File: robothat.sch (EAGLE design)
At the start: 84 parts, among them IC3 78L05SMD, T1 BC847, U1 LM293AD, U2 TSM2312CX, U3 ADUM7441ARQZ, U5 TSM2312CX, U8 LM293AD

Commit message: finished first place
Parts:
- removed C3: 100n, rcl:C-EUC0805
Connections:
- net AGND: no longer C3.1
- net AX12_RX: now also AXFUSE1.2
- net AX12_RX_P: no longer AXFUSE1.2
- net VCC: no longer C3.2
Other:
- moved on the sheet: AXFUSE, AXFUSE1
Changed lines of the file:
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@@
 <setting verticaltext="up"/>
 </settings>
-<grid distance="0.1" unitdist="inch" unit="inch" style="lines" multiple="1" display="no" altdistance="0.01" altunitdist="inch" altunit="inch"/>
+<grid distance="0.05" unitdist="inch" unit="inch" style="lines" multiple="1" display="no" altdistance="0.01" altunitdist="inch" altunit="inch"/>
 <layers>
 <layer number="1" name="Top" color="4" fill="1" visible="no" active="no"/>
@@
 <part name="R6" library="resistor" deviceset="R-US_" device="R0805" value="470R"/>
 <part name="R7" library="resistor" deviceset="R-US_" device="R0805" value="470R"/>
-<part name="C3" library="rcl" deviceset="C-EU" device="C0805" value="100n"/>
 <part name="GND4" library="supply1" deviceset="GND" device=""/>
 <part name="POWER" library="con-phoenix-500" deviceset="MSTBV2" device=""/>
@@
 <part name="P+22" library="supply1" deviceset="VCC" device=""/>
 <part name="P+23" library="supply1" deviceset="VCC" device=""/>
-<part name="AGND10" library="supply1" deviceset="AGND" device=""/>
 <part name="VDD1" library="supply1" deviceset="VDD" device=""/>
 <part name="VDD2" library="supply1" deviceset="VDD" device=""/>
@@
 <instance part="R6" gate="G$1" x="424.18" y="177.8" rot="R180"/>
 <instance part="R7" gate="G$1" x="424.18" y="185.42" rot="R180"/>
-<instance part="C3" gate="G$1" x="378.46" y="190.5" rot="R180"/>
 <instance part="GND4" gate="1" x="24.13" y="130.81"/>
 <instance part="POWER" gate="-1" x="281.94" y="193.04" rot="R270"/>
@@
 <instance part="GND16" gate="1" x="215.9" y="35.56"/>
 <instance part="C13" gate="G$1" x="251.46" y="43.18" rot="R180"/>
-<instance part="AXFUSE" gate="G$1" x="208.28" y="91.44" rot="R90"/>
-<instance part="AXFUSE1" gate="G$1" x="213.36" y="78.74" rot="R90"/>
+<instance part="AXFUSE" gate="G$1" x="147.32" y="157.48"/>
+<instance part="AXFUSE1" gate="G$1" x="148.59" y="165.1"/>
 <instance part="AGND1" gate="VR1" x="241.3" y="35.56"/>
 <instance part="AGND2" gate="VR1" x="251.46" y="35.56"/>
@@
 <instance part="P+22" gate="VCC" x="254" y="177.8"/>
 <instance part="P+23" gate="VCC" x="256.54" y="114.3"/>
-<instance part="AGND10" gate="VR1" x="378.46" y="182.88"/>
 <instance part="VDD1" gate="G$1" x="330.2" y="142.24"/>
 <instance part="VDD2" gate="G$1" x="292.1" y="187.96"/>
@@
 <segment>
 <pinref part="U3" gate="A" pin="VOC"/>
-<wire x1="213.36" y1="101.6" x2="210.82" y2="101.6" width="0.1524" layer="91"/>
 <label x="195.58" y="101.6" size="1.778" layer="95"/>
-<pinref part="AXFUSE1" gate="G$1" pin="2"/>
-<wire x1="210.82" y1="101.6" x2="208.28" y2="101.6" width="0.1524" layer="91"/>
-<wire x1="213.36" y1="83.82" x2="213.36" y2="96.52" width="0.1524" layer="91"/>
-<wire x1="213.36" y1="96.52" x2="210.82" y2="96.52" width="0.1524" layer="91"/>
-<wire x1="210.82" y1="96.52" x2="210.82" y2="101.6" width="0.1524" layer="91"/>
-<junction x="210.82" y="101.6"/>
+<wire x1="213.36" y1="101.6" x2="208.28" y2="101.6" width="0.1524" layer="91"/>
 </segment>
 </net>
@@
 <segment>
 <pinref part="AXFUSE1" gate="G$1" pin="1"/>
-<wire x1="213.36" y1="73.66" x2="205.74" y2="73.66" width="0.1524" layer="91"/>
-<label x="195.58" y="73.66" size="1.778" layer="95" ratio="12"/>
+<wire x1="143.51" y1="165.1" x2="139.7" y2="165.1" width="0.1524" layer="91"/>
+<label x="129.54" y="165.1" size="1.778" layer="95" ratio="12"/>
 </segment>
 </net>
@@
 <segment>
 <pinref part="AXFUSE" gate="G$1" pin="1"/>
-<wire x1="208.28" y1="86.36" x2="205.74" y2="86.36" width="0.1524" layer="91"/>
-<label x="195.58" y="86.36" size="1.778" layer="95" ratio="12"/>
+<wire x1="142.24" y1="157.48" x2="139.7" y2="157.48" width="0.1524" layer="91"/>
+<label x="129.54" y="157.48" size="1.778" layer="95" ratio="12"/>
 </segment>
 </net>
@@
 <segment>
 <pinref part="AX12USB" gate="-1" pin="1"/>
-<wire x1="154.94" y1="149.86" x2="149.86" y2="149.86" width="0.1524" layer="91"/>
+<wire x1="154.94" y1="149.86" x2="152.4" y2="149.86" width="0.1524" layer="91"/>
 <label x="139.7" y="149.86" size="1.778" layer="95"/>
+<pinref part="AXFUSE" gate="G$1" pin="2"/>
+<wire x1="152.4" y1="149.86" x2="149.86" y2="149.86" width="0.1524" layer="91"/>
+<wire x1="152.4" y1="157.48" x2="152.4" y2="149.86" width="0.1524" layer="91"/>
+<junction x="152.4" y="149.86"/>
 </segment>
 <segment>
@@
 <wire x1="213.36" y1="99.06" x2="208.28" y2="99.06" width="0.1524" layer="91"/>
 <label x="198.12" y="99.06" size="1.778" layer="95"/>
-<pinref part="AXFUSE" gate="G$1" pin="2"/>
-<wire x1="208.28" y1="96.52" x2="208.28" y2="99.06" width="0.1524" layer="91"/>
 </segment>
 </net>
@@
 <segment>
 <pinref part="AX12USB" gate="-2" pin="1"/>
-<wire x1="154.94" y1="147.32" x2="149.86" y2="147.32" width="0.1524" layer="91"/>
+<wire x1="154.94" y1="147.32" x2="153.67" y2="147.32" width="0.1524" layer="91"/>
 <label x="139.7" y="147.32" size="1.778" layer="95"/>
+<pinref part="AXFUSE1" gate="G$1" pin="2"/>
+<wire x1="153.67" y1="147.32" x2="149.86" y2="147.32" width="0.1524" layer="91"/>
+<wire x1="153.67" y1="165.1" x2="153.67" y2="147.32" width="0.1524" layer="91"/>
+<junction x="153.67" y="147.32"/>
 </segment>
 <segment>
@@
 <pinref part="AGND9" gate="VR1" pin="AGND"/>
 </segment>
-<segment>
-<pinref part="C3" gate="G$1" pin="1"/>
-<wire x1="378.46" y1="187.96" x2="378.46" y2="185.42" width="0.1524" layer="91"/>
-<pinref part="AGND10" gate="VR1" pin="AGND"/>
-</segment>
 </net>
 <net name="VCC" class="0">
@@
 <pinref part="R3" gate="G$1" pin="2"/>
 <wire x1="365.76" y1="195.58" x2="365.76" y2="198.12" width="0.1524" layer="91"/>
-<wire x1="365.76" y1="198.12" x2="378.46" y2="198.12" width="0.1524" layer="91"/>
+<wire x1="365.76" y1="198.12" x2="383.54" y2="198.12" width="0.1524" layer="91"/>
 <pinref part="U1" gate="A" pin="VCC"/>
-<wire x1="378.46" y1="198.12" x2="383.54" y2="198.12" width="0.1524" layer="91"/>
 <wire x1="383.54" y1="182.88" x2="383.54" y2="198.12" width="0.1524" layer="91"/>
-<pinref part="C3" gate="G$1" pin="2"/>
-<wire x1="378.46" y1="195.58" x2="378.46" y2="198.12" width="0.1524" layer="91"/>
-<junction x="378.46" y="198.12"/>
 <pinref part="P+21" gate="VCC" pin="VCC"/>
 <junction x="383.54" y="198.12"/>

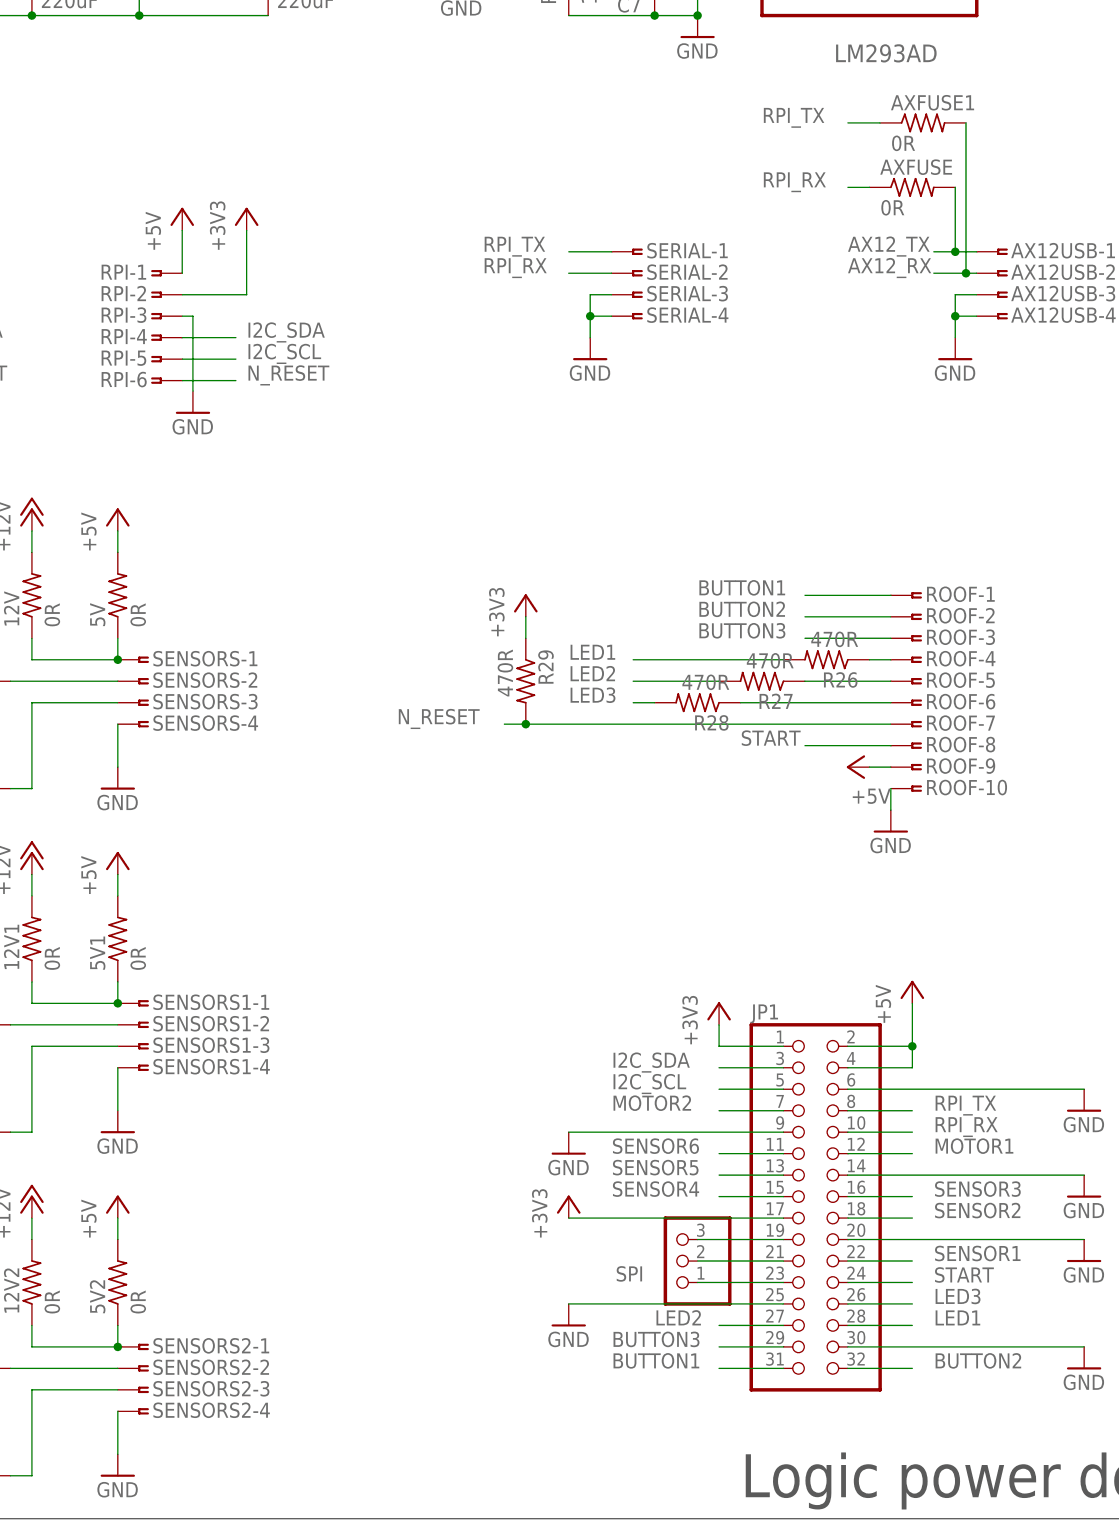
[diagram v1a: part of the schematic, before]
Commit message: routing and silkscreen done
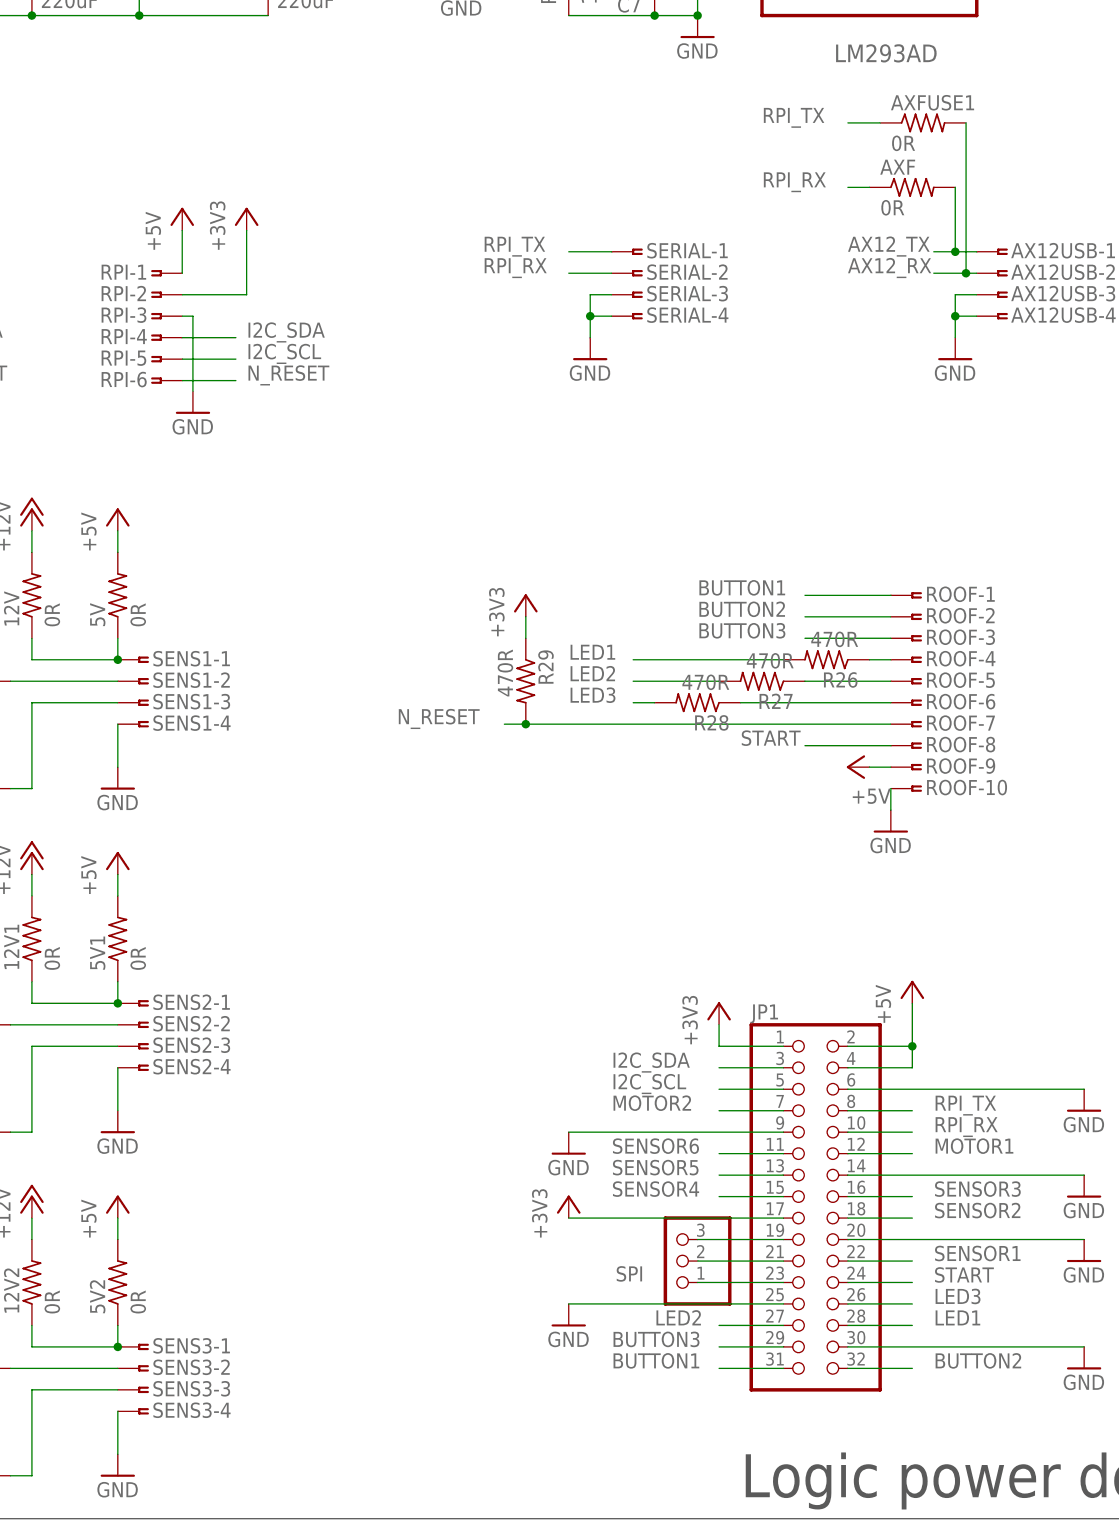
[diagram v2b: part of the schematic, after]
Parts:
- renumbered AXFUSE to AXF, SENSORS to SENS1, SENSORS1 to SENS2, SENSORS2 to SENS3
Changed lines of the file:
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@@
 <part name="AX12USB" library="con-amp" deviceset="SMDTOP-4" device=""/>
 <part name="GND7" library="supply1" deviceset="GND" device=""/>
-<part name="SENSORS" library="con-amp" deviceset="SMDTOP-4" device=""/>
+<part name="SENS1" library="con-amp" deviceset="SMDTOP-4" device=""/>
 <part name="12V" library="resistor" deviceset="R-US_" device="R0805" value="0R"/>
 <part name="P+8" library="supply1" deviceset="+12V" device=""/>
@@
 <part name="D1" library="diode" deviceset="DIODE-" device="SOD523"/>
 <part name="+3V4" library="supply1" deviceset="+3V3" device=""/>
-<part name="SENSORS1" library="con-amp" deviceset="SMDTOP-4" device=""/>
+<part name="SENS2" library="con-amp" deviceset="SMDTOP-4" device=""/>
 <part name="12V1" library="resistor" deviceset="R-US_" device="R0805" value="0R"/>
 <part name="P+12" library="supply1" deviceset="+12V" device=""/>
@@
 <part name="D4" library="diode" deviceset="DIODE-" device="SOD523"/>
 <part name="+3V6" library="supply1" deviceset="+3V3" device=""/>
-<part name="SENSORS2" library="con-amp" deviceset="SMDTOP-4" device=""/>
+<part name="SENS3" library="con-amp" deviceset="SMDTOP-4" device=""/>
 <part name="12V2" library="resistor" deviceset="R-US_" device="R0805" value="0R"/>
 <part name="P+17" library="supply1" deviceset="+12V" device=""/>
@@
 <part name="GND16" library="supply1" deviceset="GND" device=""/>
 <part name="C13" library="rcl" deviceset="C-EU" device="C0805" value="100n"/>
-<part name="AXFUSE" library="resistor" deviceset="R-US_" device="R0805" value="0R"/>
+<part name="AXF" library="resistor" deviceset="R-US_" device="R0805" value="0R"/>
 <part name="AXFUSE1" library="resistor" deviceset="R-US_" device="R0805" value="0R"/>
 <part name="AGND1" library="supply1" deviceset="AGND" device=""/>
@@
 <instance part="AX12USB" gate="-4" x="157.48" y="142.24"/>
 <instance part="GND7" gate="1" x="152.4" y="137.16"/>
-<instance part="SENSORS" gate="-1" x="55.88" y="101.6"/>
-<instance part="SENSORS" gate="-2" x="55.88" y="99.06"/>
-<instance part="SENSORS" gate="-3" x="55.88" y="96.52"/>
-<instance part="SENSORS" gate="-4" x="55.88" y="93.98"/>
+<instance part="SENS1" gate="-1" x="55.88" y="101.6"/>
+<instance part="SENS1" gate="-2" x="55.88" y="99.06"/>
+<instance part="SENS1" gate="-3" x="55.88" y="96.52"/>
+<instance part="SENS1" gate="-4" x="55.88" y="93.98"/>
 <instance part="12V" gate="G$1" x="43.18" y="109.22" rot="R90"/>
 <instance part="P+8" gate="1" x="43.18" y="119.38"/>
@@
 <instance part="D1" gate="G$1" x="27.94" y="101.6" rot="R90"/>
 <instance part="+3V4" gate="G$1" x="27.94" y="109.22"/>
-<instance part="SENSORS1" gate="-1" x="55.88" y="60.96"/>
-<instance part="SENSORS1" gate="-2" x="55.88" y="58.42"/>
-<instance part="SENSORS1" gate="-3" x="55.88" y="55.88"/>
-<instance part="SENSORS1" gate="-4" x="55.88" y="53.34"/>
+<instance part="SENS2" gate="-1" x="55.88" y="60.96"/>
+<instance part="SENS2" gate="-2" x="55.88" y="58.42"/>
+<instance part="SENS2" gate="-3" x="55.88" y="55.88"/>
+<instance part="SENS2" gate="-4" x="55.88" y="53.34"/>
 <instance part="12V1" gate="G$1" x="43.18" y="68.58" rot="R90"/>
 <instance part="P+12" gate="1" x="43.18" y="78.74"/>
@@
 <instance part="D4" gate="G$1" x="27.94" y="60.96" rot="R90"/>
 <instance part="+3V6" gate="G$1" x="27.94" y="68.58"/>
-<instance part="SENSORS2" gate="-1" x="55.88" y="20.32"/>
-<instance part="SENSORS2" gate="-2" x="55.88" y="17.78"/>
-<instance part="SENSORS2" gate="-3" x="55.88" y="15.24"/>
-<instance part="SENSORS2" gate="-4" x="55.88" y="12.7"/>
+<instance part="SENS3" gate="-1" x="55.88" y="20.32"/>
+<instance part="SENS3" gate="-2" x="55.88" y="17.78"/>
+<instance part="SENS3" gate="-3" x="55.88" y="15.24"/>
+<instance part="SENS3" gate="-4" x="55.88" y="12.7"/>
 <instance part="12V2" gate="G$1" x="43.18" y="27.94" rot="R90"/>
 <instance part="P+17" gate="1" x="43.18" y="38.1"/>
@@
 <instance part="GND16" gate="1" x="215.9" y="35.56"/>
 <instance part="C13" gate="G$1" x="251.46" y="43.18" rot="R180"/>
-<instance part="AXFUSE" gate="G$1" x="147.32" y="157.48"/>
+<instance part="AXF" gate="G$1" x="147.32" y="157.48"/>
 <instance part="AXFUSE1" gate="G$1" x="148.59" y="165.1"/>
 <instance part="AGND1" gate="VR1" x="241.3" y="35.56"/>
@@
 <segment>
 <pinref part="GND8" gate="1" pin="GND"/>
-<pinref part="SENSORS" gate="-4" pin="1"/>
+<pinref part="SENS1" gate="-4" pin="1"/>
 <wire x1="53.34" y1="88.9" x2="53.34" y2="93.98" width="0.1524" layer="91"/>
 </segment>
 <segment>
 <pinref part="GND9" gate="1" pin="GND"/>
-<pinref part="SENSORS1" gate="-4" pin="1"/>
+<pinref part="SENS2" gate="-4" pin="1"/>
 <wire x1="53.34" y1="48.26" x2="53.34" y2="53.34" width="0.1524" layer="91"/>
 </segment>
 <segment>
 <pinref part="GND10" gate="1" pin="GND"/>
-<pinref part="SENSORS2" gate="-4" pin="1"/>
+<pinref part="SENS3" gate="-4" pin="1"/>
 <wire x1="53.34" y1="7.62" x2="53.34" y2="12.7" width="0.1524" layer="91"/>
 </segment>
@@
 </segment>
 <segment>
-<pinref part="AXFUSE" gate="G$1" pin="1"/>
+<pinref part="AXF" gate="G$1" pin="1"/>
 <wire x1="142.24" y1="157.48" x2="139.7" y2="157.48" width="0.1524" layer="91"/>
 <label x="129.54" y="157.48" size="1.778" layer="95" ratio="12"/>
@@
 <wire x1="154.94" y1="149.86" x2="152.4" y2="149.86" width="0.1524" layer="91"/>
 <label x="139.7" y="149.86" size="1.778" layer="95"/>
-<pinref part="AXFUSE" gate="G$1" pin="2"/>
+<pinref part="AXF" gate="G$1" pin="2"/>
 <wire x1="152.4" y1="149.86" x2="149.86" y2="149.86" width="0.1524" layer="91"/>
 <wire x1="152.4" y1="157.48" x2="152.4" y2="149.86" width="0.1524" layer="91"/>
@@
 <net name="N$9" class="0">
 <segment>
-<pinref part="SENSORS" gate="-1" pin="1"/>
+<pinref part="SENS1" gate="-1" pin="1"/>
 <pinref part="12V" gate="G$1" pin="1"/>
 <wire x1="53.34" y1="101.6" x2="43.18" y2="101.6" width="0.1524" layer="91"/>
@@
 <segment>
 <pinref part="R19" gate="G$1" pin="1"/>
-<pinref part="SENSORS" gate="-2" pin="1"/>
+<pinref part="SENS1" gate="-2" pin="1"/>
 <wire x1="40.64" y1="99.06" x2="53.34" y2="99.06" width="0.1524" layer="91"/>
 </segment>
@@
 <wire x1="40.64" y1="86.36" x2="43.18" y2="86.36" width="0.1524" layer="91"/>
 <wire x1="43.18" y1="86.36" x2="43.18" y2="96.52" width="0.1524" layer="91"/>
-<pinref part="SENSORS" gate="-3" pin="1"/>
+<pinref part="SENS1" gate="-3" pin="1"/>
 <wire x1="43.18" y1="96.52" x2="53.34" y2="96.52" width="0.1524" layer="91"/>
 </segment>
@@
 <net name="N$10" class="0">
 <segment>
-<pinref part="SENSORS1" gate="-1" pin="1"/>
+<pinref part="SENS2" gate="-1" pin="1"/>
 <pinref part="12V1" gate="G$1" pin="1"/>
 <wire x1="53.34" y1="60.96" x2="43.18" y2="60.96" width="0.1524" layer="91"/>
@@
 <segment>
 <pinref part="R22" gate="G$1" pin="1"/>
-<pinref part="SENSORS1" gate="-2" pin="1"/>
+<pinref part="SENS2" gate="-2" pin="1"/>
 <wire x1="40.64" y1="58.42" x2="53.34" y2="58.42" width="0.1524" layer="91"/>
 </segment>
@@
 <wire x1="40.64" y1="45.72" x2="43.18" y2="45.72" width="0.1524" layer="91"/>
 <wire x1="43.18" y1="45.72" x2="43.18" y2="55.88" width="0.1524" layer="91"/>
-<pinref part="SENSORS1" gate="-3" pin="1"/>
+<pinref part="SENS2" gate="-3" pin="1"/>
 <wire x1="43.18" y1="55.88" x2="53.34" y2="55.88" width="0.1524" layer="91"/>
 </segment>
@@
 <net name="N$26" class="0">
 <segment>
-<pinref part="SENSORS2" gate="-1" pin="1"/>
+<pinref part="SENS3" gate="-1" pin="1"/>
 <pinref part="12V2" gate="G$1" pin="1"/>
 <wire x1="53.34" y1="20.32" x2="43.18" y2="20.32" width="0.1524" layer="91"/>
@@
 <segment>
 <pinref part="R24" gate="G$1" pin="1"/>
-<pinref part="SENSORS2" gate="-2" pin="1"/>
+<pinref part="SENS3" gate="-2" pin="1"/>
 <wire x1="40.64" y1="17.78" x2="53.34" y2="17.78" width="0.1524" layer="91"/>
 </segment>
@@
 <wire x1="40.64" y1="5.08" x2="43.18" y2="5.08" width="0.1524" layer="91"/>
 <wire x1="43.18" y1="5.08" x2="43.18" y2="15.24" width="0.1524" layer="91"/>
-<pinref part="SENSORS2" gate="-3" pin="1"/>
+<pinref part="SENS3" gate="-3" pin="1"/>
 <wire x1="43.18" y1="15.24" x2="53.34" y2="15.24" width="0.1524" layer="91"/>
 </segment>
